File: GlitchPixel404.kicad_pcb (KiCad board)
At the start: 2 copper layers, 50 x 34 mm, 71 parts, among them J1 Barrel_Jack_Switch, J2 USB_C_Receptacle_USB2.0_16P, J3 Output, J4 VOLTLINK, J5 Conn_01x03, Q1 MMBT3904, Q2 AONR21357-ES, SW1 SW_SP3T, SW3 Reset, SW4 Boot, U1 74LVC2G34, U2 TPS54202DDC, U3 CH224K, U4 74LVC2G34, U5 HE2021A50HMR, U6 ESP32-PICO-MINI-02U-N8R2, U7 IRM-H6xxT

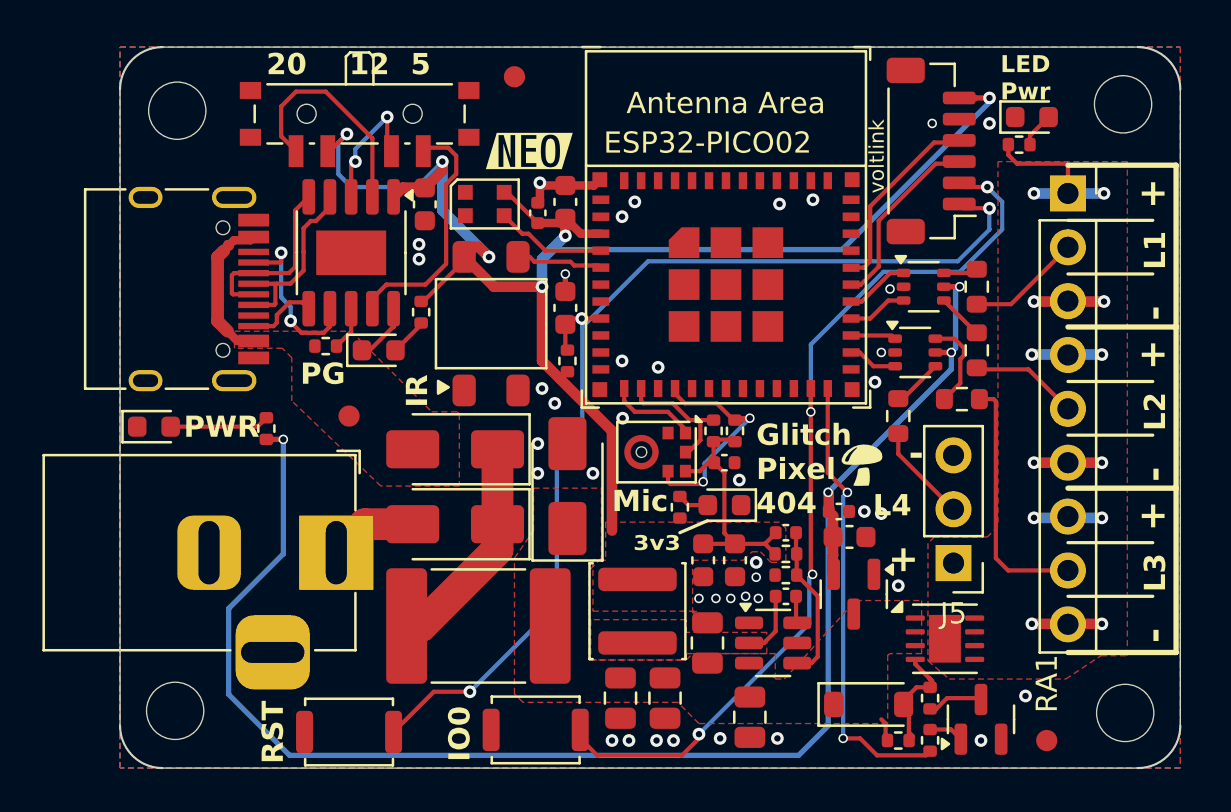
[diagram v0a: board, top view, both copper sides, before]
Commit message: Adjusted component selection
Final silk and checks before prototype batch ready
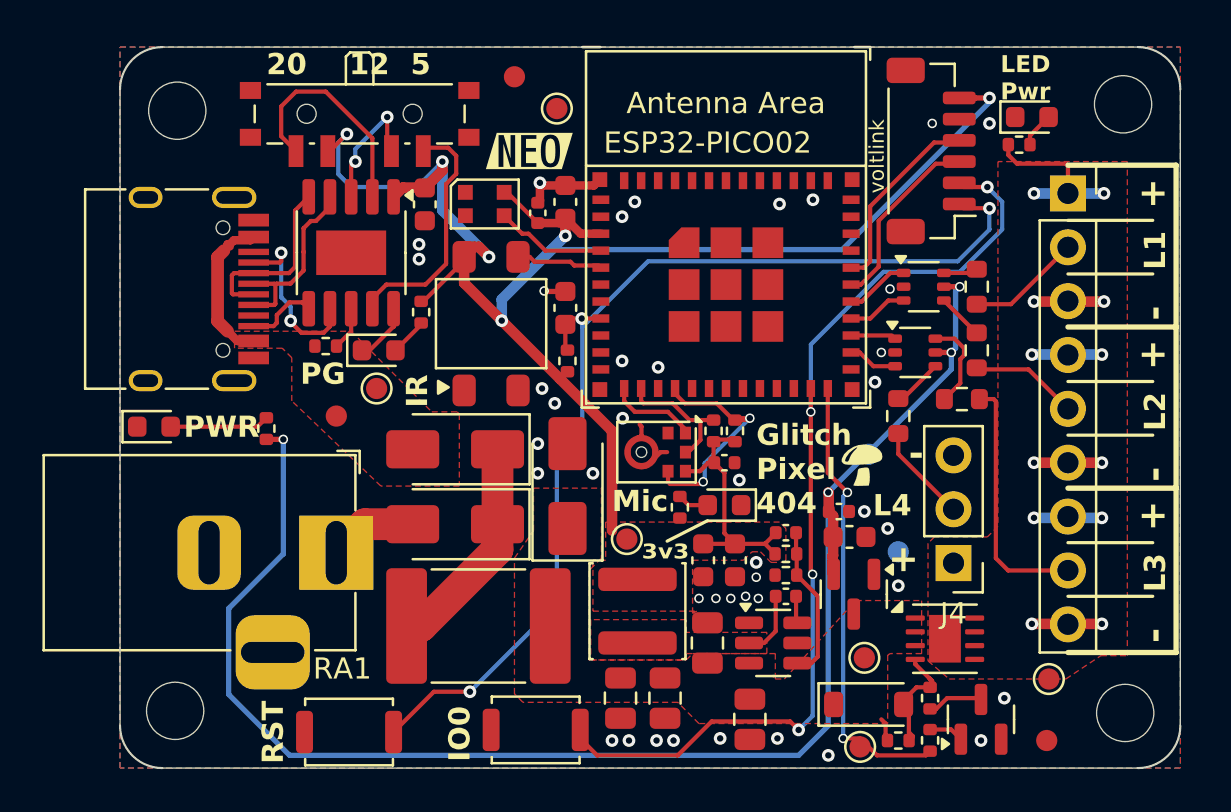
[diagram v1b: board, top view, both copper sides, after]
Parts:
- added TPr1: Vcc, TestPoint:TestPoint_Pad_D1.0mm, F.Cu at (135.1, 94.8)
- added TPr2: Vbus, TestPoint:TestPoint_Pad_D1.0mm, F.Cu at (112.1, 82.1)
- added TPr3: 3v3, TestPoint:TestPoint_Pad_D1.0mm, F.Cu at (123.9, 89.2)
- added TPr4: Gnd, TestPoint:TestPoint_Pad_D1.0mm, F.Cu at (120.6, 68.9)
- added TPr5: LPWR, TestPoint:TestPoint_Pad_D1.0mm, F.Cu at (143.8, 95.8)
- added TPr6: 5v, TestPoint:TestPoint_Pad_D1.0mm, B.Cu at (135.3, 85.2)
- added TPr7: Gnd, TestPoint:TestPoint_Pad_D1.0mm, B.Cu at (136.7, 89.8)
- added TPr8: SLPwr, TestPoint:TestPoint_Pad_D1.0mm, F.Cu at (134.9, 99.0)
- D4: value Yellow -> Red
- D6: renamed from D9; value Yellow -> Red
- D8: value Green -> Red
- D9: renamed from D7; value Green -> Red
- U3: renamed from U7; value IRM-H6xxT -> IRM-H638T/TR2
- moved FID2 0.60 mm to (110.2, 83.4)
- moved C14 0.10 mm to (129.7, 97.7)
- renumbered C6 to C1, C1 to C11, C16 to C12, C11 to C14, C13 to C15, C2 to C16, C8 to C2, C14 to C3, C15 to C4, C12 to C5, C4 to C6, C3 to C7, C5 to C8, C7 to C9, D3 to D2, D2 to D3, D6 to D7, H3 to H2, H2 to H3, J4 to J3, J5 to J4, J3 to J5, Q2 to Q1, Q1 to Q2, R11 to R1, R15 to R10, R16 to R11, R14 to R12, R12 to R13, R1 to R14, R8 to R15, R2 to R16, R9 to R17, R3 to R2, R19 to R3, R20 to R4, R18 to R7, R13 to R8, R17 to R9, SW3 to SW1, SW4 to SW2, SW1 to SW3, U3 to U1, U6 to U2, U2 to U4, U1 to U6, U4 to U7
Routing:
- net GND: track 14.5 -> 20.6 mm, vias 46 -> 47
- net /IO0: track 42.9 -> 45.7 mm
- net +3.3V: track 85.0 -> 86.1 mm

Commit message: RevA1
Sent for manufacture of prototypes
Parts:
- added G***: LOGO, LOGO, B.Cu at (122.1, 89.9)
- added TPr10: Rx, TestPoint:TestPoint_Pad_D1.0mm, B.Cu at (138.1, 73.3)
- added TPr9: Tx, TestPoint:TestPoint_Pad_D1.0mm, B.Cu at (136.8, 69.3)
- J5: footprint Connector_PinSocket_2.54mm:PinSocket_1x09_P2.54mm_Vertical -> Inventel:CONN-TH_9P-P2.54_MX128-2.54-09P-GN01-CU-Y-A
- moved FID2 36.9 mm to (144.5, 69.8)
- moved G*** 16.8 mm to (142.8, 69.8)
- moved J5 10.2 mm to (144.7, 83.1), turned to 90 degrees
- moved D9 1.46 mm to (142.6, 67.9), turned to -90 degrees
- moved kibuzzard-67E14B7B 0.30 mm to (119.6, 70.9)
- moved R9 0.22 mm to (142.6, 70.5), turned to 90 degrees
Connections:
- net SCL renamed MIC_SCK
- net SDA renamed MIC_SDA
- D5 pad 3: /NEO_OB -> NEO_OB
- J5 pad 1: LED_PWR -> GND
- J5 pad 2: L1 -> L3
- J5 pad 3: GND -> LED_PWR
- J5 pad 4: LED_PWR -> GND
- J5 pad 6: GND -> LED_PWR
- J5 pad 7: LED_PWR -> GND
- J5 pad 8: L3 -> L1
- J5 pad 9: GND -> LED_PWR
- U2 pad 16: unconnected-(U2-GPIO26/ADC2_CH9/DAC_2-Pad16) -> S2
- U2 pad 17: unconnected-(U2-GPIO27/ADC2_CH7-Pad17) -> S3
- U2 pad 27: S3 -> unconnected-(U2-SD_DATA_0/GPIO7-Pad27)
- U2 pad 28: S2 -> unconnected-(U2-SD_DATA_1/GPIO8-Pad28)
- U2 pad 29: S1 -> unconnected-(U2-GPIO5-Pad29)
- U2 pad 33: unconnected-(U2-GPIO19-Pad33) -> S1
- U2 pad 34: unconnected-(U2-GPIO22-Pad34) -> NEO_OB
- U2 pad 4: /NEO_OB -> unconnected-(U2-SENSOR_VP/GPIO36/ADC1_CH0-Pad4)
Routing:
- net NEO_OB: track 0.00 -> 16.9 mm, vias 0 -> 2
- net S2: track 2.83 -> 12.0 mm, vias 0 -> 2
- net S3: track 1.93 -> 10.4 mm, vias 0 -> 2
- net /NEO_OB: track 5.24 -> 0.00 mm
- net S1: track 3.03 -> 6.53 mm, vias 0 -> 2
- net /RXD: track 8.63 -> 11.2 mm, vias 0 -> 1
- net /IO0: track 45.7 -> 48.0 mm
- net /TXD: track 8.96 -> 11.2 mm, vias 0 -> 1
- net GND: track 20.6 -> 18.4 mm, vias 47 -> 50
- net LED_PWR: track 14.5 -> 13.3 mm
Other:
- board text added: "!!CAUTION!! Match Volts With LEDs!"
- board text added: "0"
- board text added: "19"
- board text added: "22"
- board text added: "26"
- board text added: "27"
- board text added: "3"
- board text added: "5-24V"
- board text added: "Ash<3"
- board text added: "BT0"
- board text added: "CH224"
- board text added: "Camp404 Special Edition Meow!"
- board text added: "E"
- board text added: "Fused 5A!"
- board text added: "G"
- board text added: "GP404A1_"
- board text added: "GlitchPixel404"
- board text added: "Inventel 2025 - RBM"
- board text added: "LED Sigs 5V Buff'd"
- board text added: "Lp"
- board text added: "Meow!Meow!Meow!"
- board text added: "Mic=ICS43434 I2S WS:32 SCK:25 SDA:33"
- board text added: "R"
- board text added: "RevA1"
- board text added: "Select:"
- board text added: "T"
- board text added: "USB PD"
- board text added: "USB PD Support"
- board text added: "VB"
- board text added: "Vc"
- board text added: "ben@inventel.co.za"
- board text added: "github.com/ramb0t/GlitchPixel404"
- board text added: "or the magic smoke will come out xD dont say I didn't warn you ^.^"
- board text added: "sLp"
- board text added: "volt"
- board text removed: "IO0"
- board text removed: "JLCJLCJLC"
- board text removed: "L1"
- board text removed: "L2"
- board text removed: "L3"
- board text removed: "L4"
